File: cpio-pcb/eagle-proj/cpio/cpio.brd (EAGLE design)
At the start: 100 x 80 mm, 76 parts

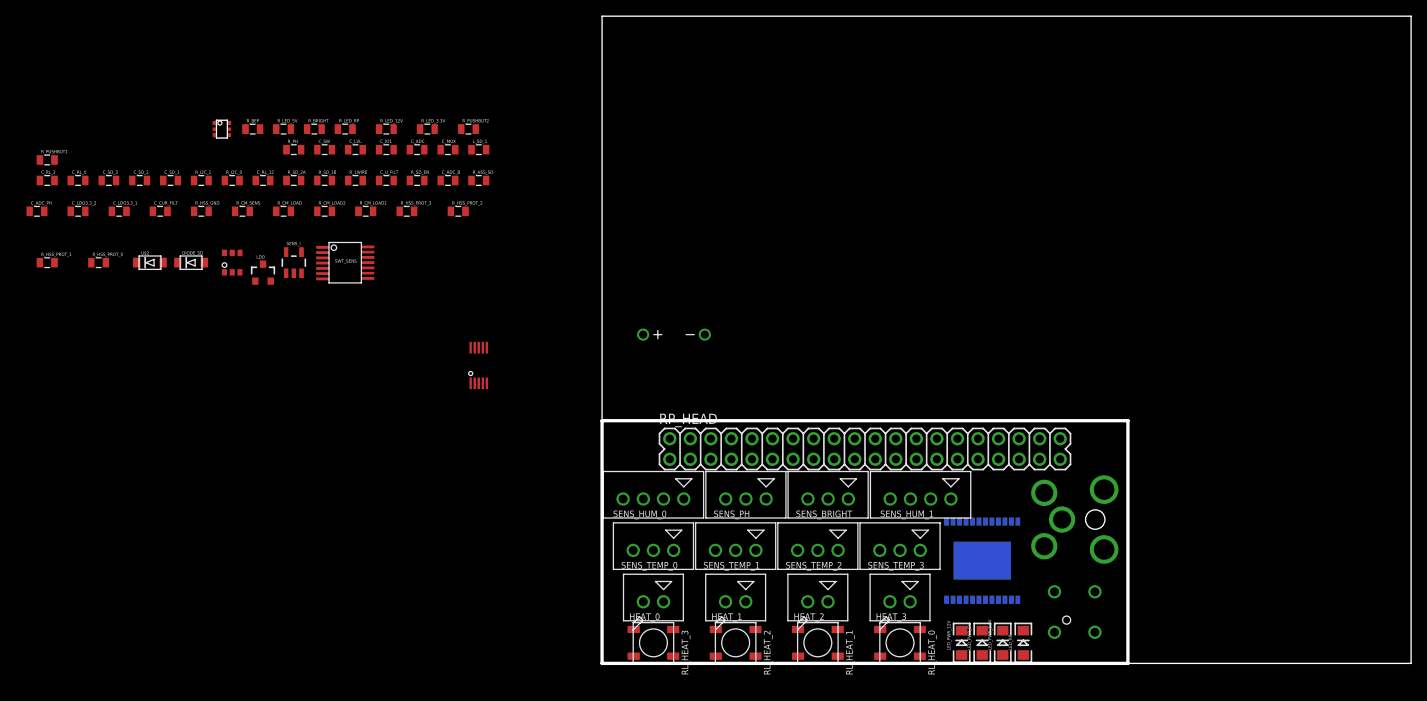
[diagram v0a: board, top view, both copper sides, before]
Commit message: schematic revised and first BOM
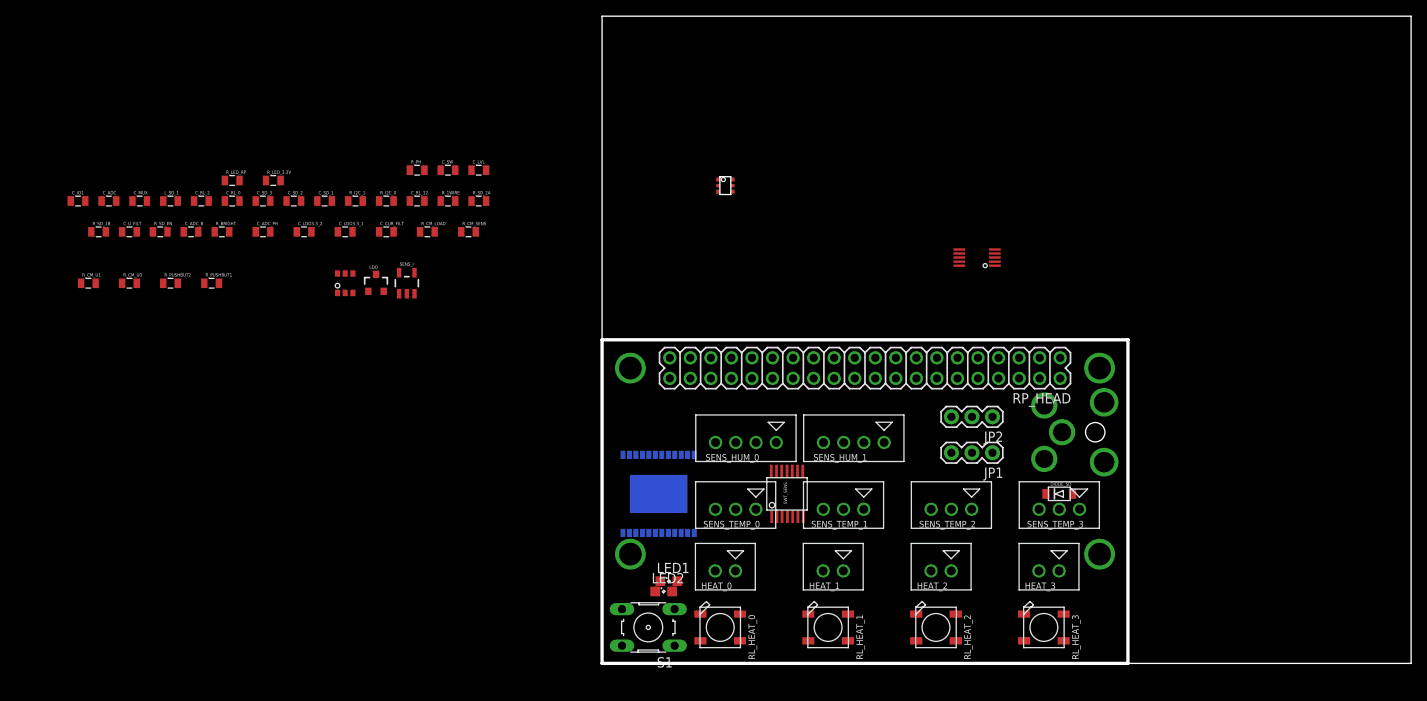
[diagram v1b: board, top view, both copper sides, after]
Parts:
- removed BEEP: BEEPER, cpio:BEEPER
- removed LED_PWR_12V, LED_PWR_3.3V, LED_PWR_5V, LED_RP: (no value), SparkFun-LED:LED-1206
- removed PUSH1: BUTTON, cpio:BUTTON
- removed R_BEP, R_LED_12V, R_LED_5V: (no value), SparkFun-Passives:0805
- removed R_CM_LOAD1, R_CM_LOAD2: 100, SparkFun-Passives:0805
- removed R_HSS_GND: 1k, SparkFun-Passives:0805
- removed R_HSS_PROT_0, R_HSS_PROT_1, R_HSS_PROT_2, R_HSS_PROT_3, R_HSS_SD: 10k, SparkFun-Passives:0805
- removed SENS_BRIGHT, SENS_PH: XH-A-3, cpio:XH-A-3
- removed U$2: DB2X41100L, cpio:SOD-123FL
- added JP1, JP2: (no value), SparkFun-Connectors:1X03
- added LED1, LED2: (no value), led:SML0805
- added R_CM_U0: 10k, SparkFun-Passives:0805
- added R_CM_U1: 1k, SparkFun-Passives:0805
- added S1: (no value), switch-omron:B3F-10XX
- added U$3, U$4, U$5, U$6: SPACERHOLE, cpio:HOLE
- C_SD_1: value 4.7u -> 10u
- C_SD_3: value 10n -> 100n
- R_BRIGHT, R_LED_3.3V, R_LED_RP, R_PUSHBUT1: value (none) -> 1k
- R_CM_LOAD: value 100 -> 10k
- R_CM_SENS: value 1m -> 10m
- R_PH: value 10k -> 1k
- R_PUSHBUT2: value (none) -> 100
- moved DIODE_SD 111.1 mm to (56.5, 21.0)
- moved ADC 63.0 mm to (46.4, 50.2), turned to 90 degrees
- moved U$1 62.6 mm to (15.2, 59.1)
- moved SWT_SENS 61.6 mm to (22.9, 21.0), turned to 90 degrees
- moved RL_HEAT_3 48.3 mm to (54.6, 4.45)
- moved R_PUSHBUT2 41.5 mm to (-53.3, 47.0)
- moved SWT_HEAT 40.8 mm to (6.99, 21.0), turned to 180 degrees
- moved C_IO1 38.6 mm to (-64.8, 57.1)
- moved C_MUX 38.6 mm to (-57.1, 57.1)
- moved C_ADC 38.6 mm to (-61.0, 57.1)
- moved L_SD_1 38.6 mm to (-53.3, 57.1)
- moved C_ADC_B 32.4 mm to (-50.8, 53.3)
- moved C_U_FILT 32.4 mm to (-58.4, 53.3)
- moved R_SD_EN 32.4 mm to (-54.6, 53.3)
- moved R_SD_1B 28.7 mm to (-62.2, 53.3)
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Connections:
- removed net GPIO17: BEEP.-
- removed net N$11: LED_PWR_5V.A, R_LED_5V.1
- removed net N$23: U$2.A
- removed net N$30: R_HSS_SD.1, SWT_HEAT.11
- removed net N$31: R_HSS_PROT_3.2, SWT_HEAT.9
- removed net N$32: R_HSS_PROT_2.2, SWT_HEAT.7
- removed net N$33: R_HSS_PROT_1.2, SWT_HEAT.5
- removed net N$34: R_HSS_PROT_0.2, SWT_HEAT.3
- removed net N$4: R_HSS_GND.1, SWT_HEAT.2, SWT_HEAT.PAD
- removed net N$5: PUSH1.2, PUSH1.4, R_PUSHBUT2.1
- removed net N$64: BEEP.+, R_BEP.1
- net 12V: now also R_CM_U0.2; no longer R_CM_LOAD1.2, R_LED_12V.2
- net 3.3V: now also JP1.1, JP2.1; no longer R_BEP.2, R_HSS_SD.2, SENS_BRIGHT.1, SENS_PH.1
- net 5V: no longer R_LED_5V.2
- net ADC_U: now also R_CM_U0.1, R_CM_U1.2; no longer R_CM_LOAD1.1, R_CM_LOAD2.2
- net GND: now also JP1.3, JP2.3, LED1.C, LED2.C, R_CM_U1.1, S1.3, S1.4, SWT_HEAT.2, SWT_HEAT.PAD; no longer LED_PWR_12V.C, LED_PWR_3.3V.C, LED_PWR_5V.C, LED_RP.C, PUSH1.1, PUSH1.3, R_CM_LOAD2.1, R_HSS_GND.2, SENS_BRIGHT.3, SENS_PH.3
- net GPIO13: now also SWT_HEAT.3; no longer R_HSS_PROT_0.1
- net GPIO19: now also SWT_HEAT.5; no longer R_HSS_PROT_1.1
- net GPIO21: now also SWT_HEAT.9; no longer R_HSS_PROT_3.1
- net GPIO26: now also SWT_HEAT.7; no longer R_HSS_PROT_2.1
- net N$15: now also LED2.A; no longer LED_PWR_3.3V.A
- net N$2: now also R_PUSHBUT2.1, S1.1, S1.2; no longer LED_PWR_12V.A, R_LED_12V.1
- net N$20: now also LED1.A; no longer LED_RP.A
- net N$24: no longer U$2.C
- net N$35: now also JP1.2; no longer SENS_BRIGHT.2
- net N$7: now also JP2.2; no longer SENS_PH.2
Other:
- outline, holes or cut-outs redrawn

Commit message: schematic revs...
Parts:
- added R_BRIGHT1, R_BRIGHT2: 1k, SparkFun-Passives:0805
- moved HEAT_0 5.24 mm to (16.5, 6.35), turned to 90 degrees
- moved SENS_TEMP_0 3.81 mm to (16.5, 15.2), turned to 90 degrees
- moved SWT_SENS 3.17 mm to (22.9, 17.8), flipped to the bottom
- moved SENS_HUM_0 1.80 mm to (16.5, 26.0), turned to 90 degrees
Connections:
- net 3.3V: now also R_BRIGHT2.2
- net ADC_BRIGHT: now also R_BRIGHT1.2
- net GND: now also R_BRIGHT1.1
- net N$35: now also R_BRIGHT2.1
